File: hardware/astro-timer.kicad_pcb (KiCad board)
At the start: 2 copper layers, 65.8 x 41.4 mm, 29 parts, among them J1 AVR-ISP-6, J2 AudioJack3, Q1 Q_NPN_BEC, Q2 Q_NPN_BEC, SW1 SW_SPST, SW2 SW_Push, SW3 SW_Push, SW4 Rotary_Encoder_Switch, U1 ATmega328P-AU, Y1 Crystal

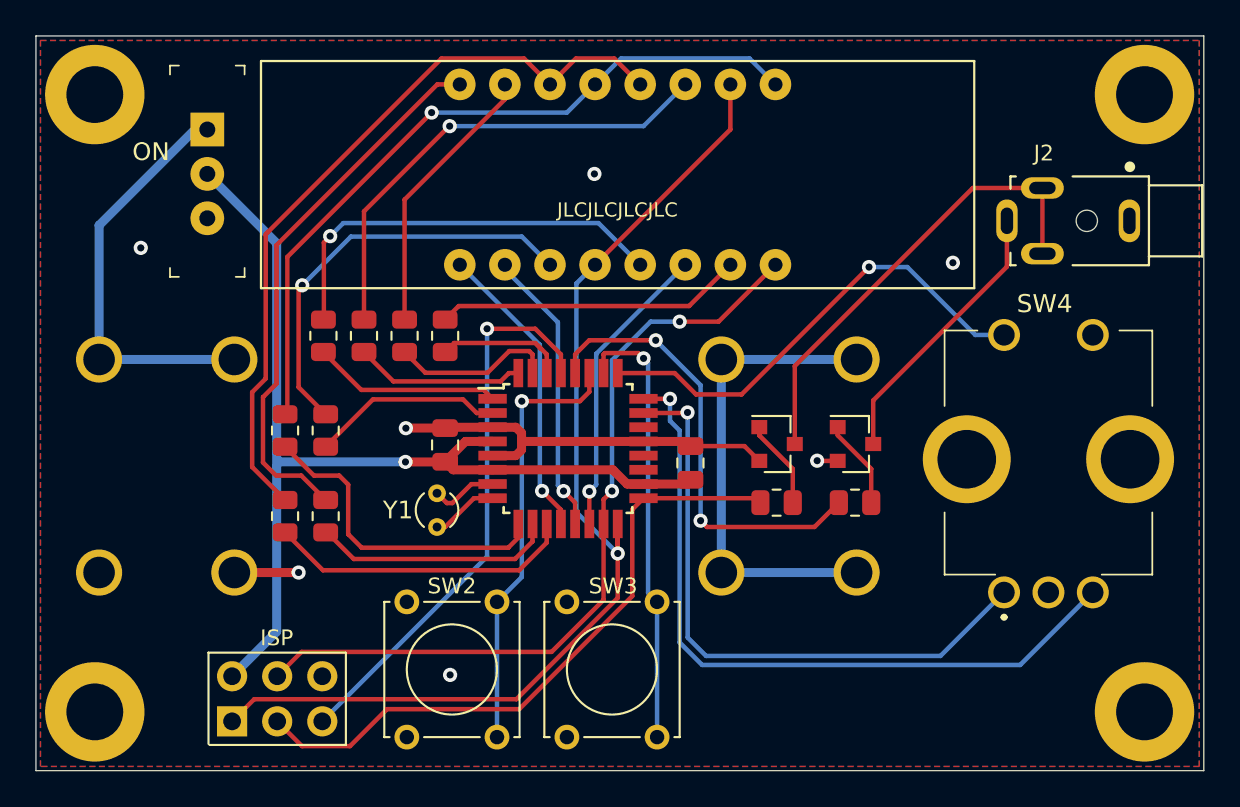
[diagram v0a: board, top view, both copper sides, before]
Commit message: add RC filter circuit for rotary encoder
seems to work pretty well on a breadboard anyway
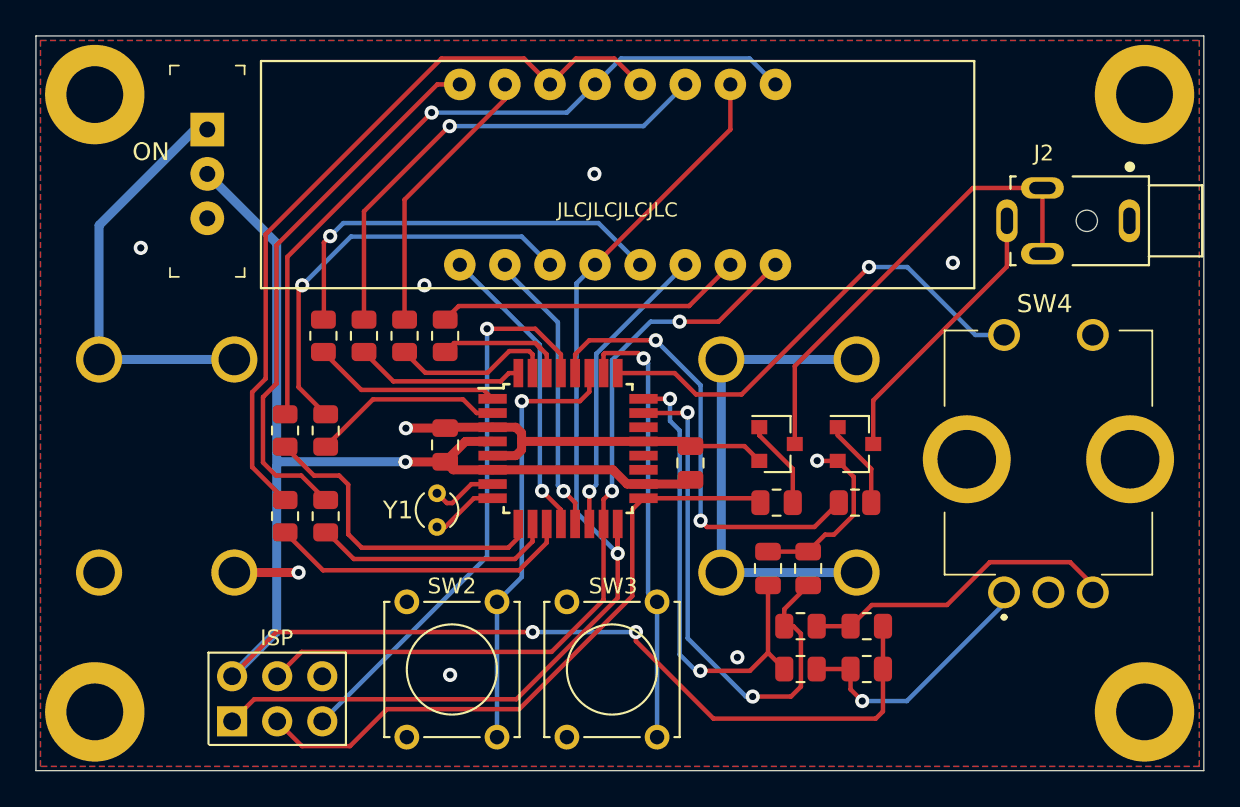
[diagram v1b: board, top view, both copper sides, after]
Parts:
- added C3: 10nF, Capacitor_SMD:C_0805_2012Metric, F.Cu at (123.7, 116.8)
- added C4: 10nF, Capacitor_SMD:C_0805_2012Metric, F.Cu at (125.9, 116.8)
- added R11: 10K, Resistor_SMD:R_0805_2012Metric, F.Cu at (125.5, 120.1)
- added R12: 10K, Resistor_SMD:R_0805_2012Metric, F.Cu at (125.5, 122.5)
- added R13: 10K, Resistor_SMD:R_0805_2012Metric, F.Cu at (129.2, 120.1)
- added R14: 10K, Resistor_SMD:R_0805_2012Metric, F.Cu at (129.2, 122.5)
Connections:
- SW4 pad A: /enc_a -> Net-(R12-Pad1)
- SW4 pad B: /enc_b -> Net-(R11-Pad1)
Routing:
- net VCC: track 58.3 -> 103.2 mm, vias 1 -> 3
- net Net-(R11-Pad1): track 0.00 -> 18.0 mm
- net Net-(R12-Pad1): track 0.00 -> 14.9 mm, vias 0 -> 1
- net /enc_b: track 40.9 -> 27.0 mm, vias 1 -> 2
- net GND: track 28.1 -> 37.2 mm, vias 7 -> 9
- net /enc_a: track 34.9 -> 30.1 mm, vias 1 -> 2

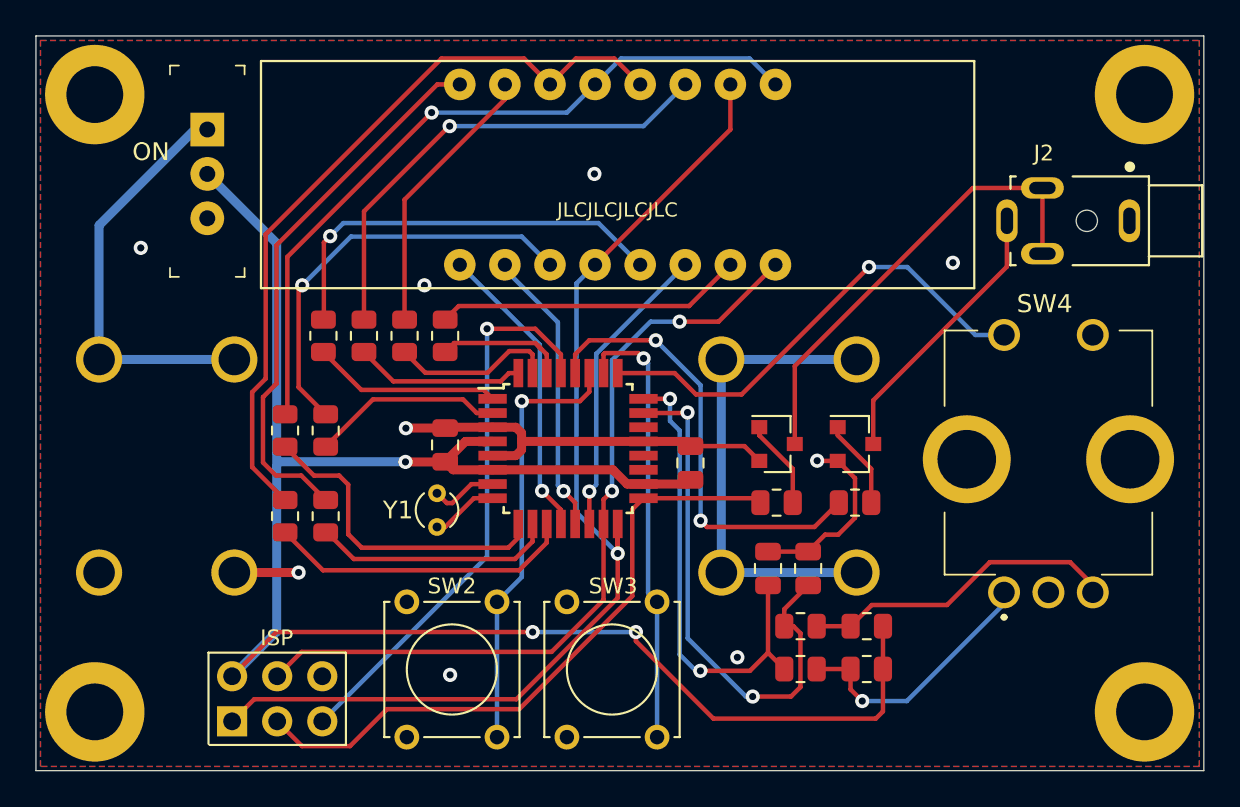
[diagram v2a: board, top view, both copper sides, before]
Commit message: felt a bit uncomfortable routing a trace under an 0805
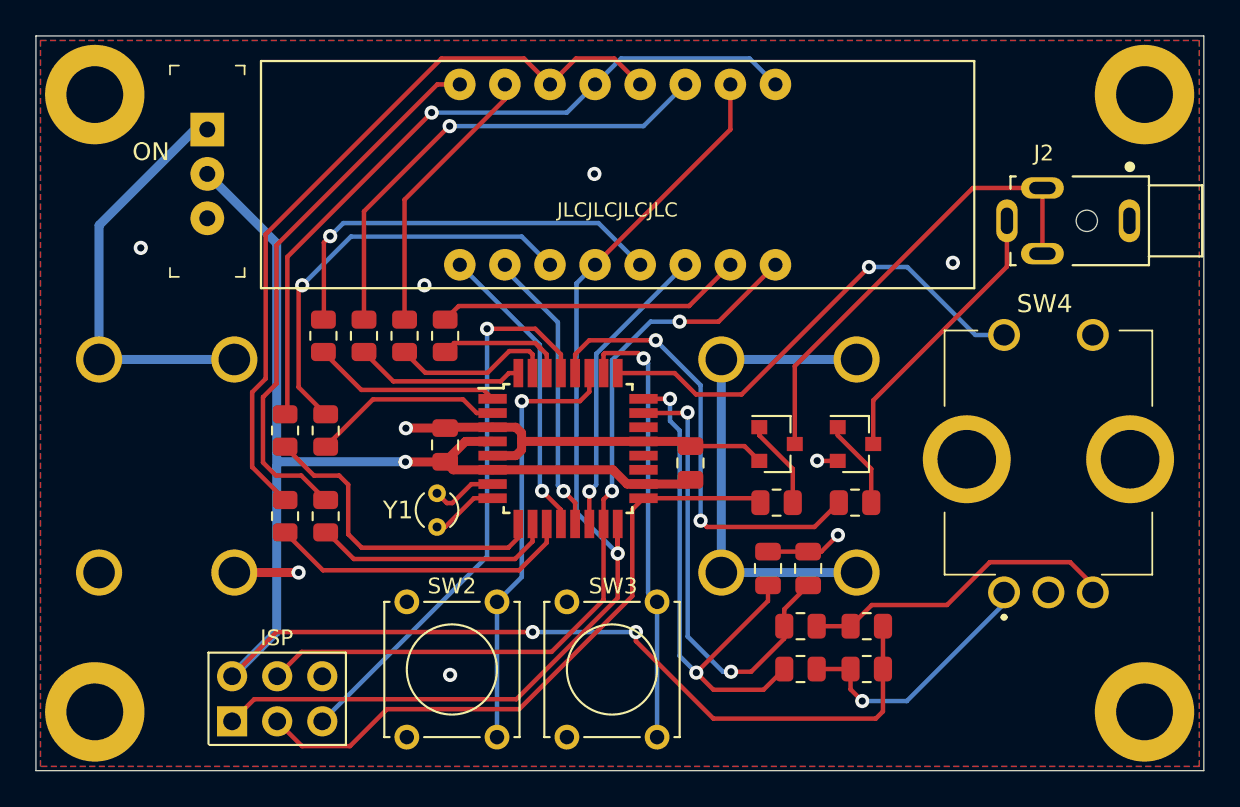
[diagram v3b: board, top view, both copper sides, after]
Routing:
- net GND: track 37.4 -> 32.4 mm
- net /enc_a: track 30.1 -> 25.7 mm
- net /enc_b: track 27.0 -> 30.0 mm

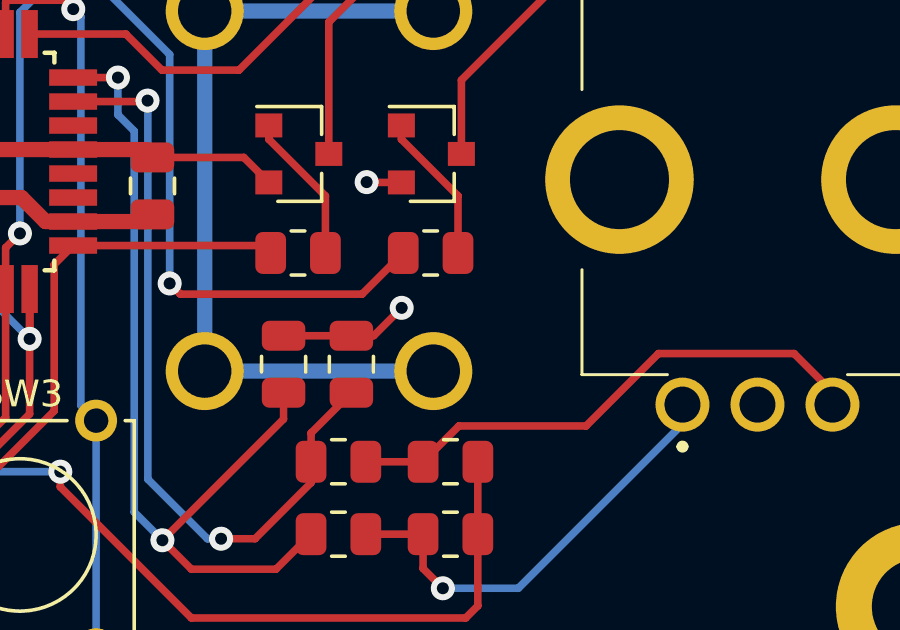
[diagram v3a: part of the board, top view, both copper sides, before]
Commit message: lol whoops that via can't be there
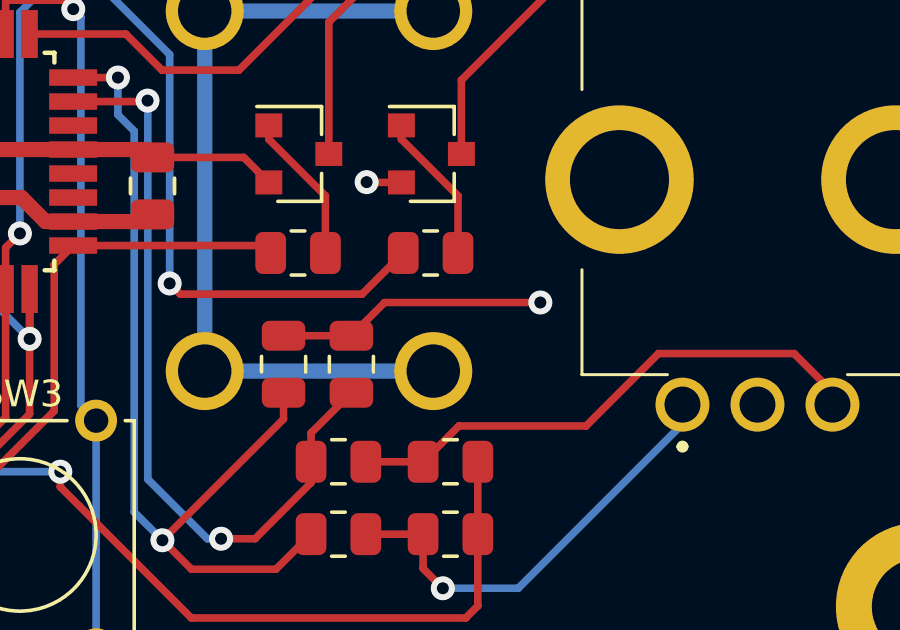
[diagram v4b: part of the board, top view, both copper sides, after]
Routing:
- net GND: track 32.4 -> 37.1 mm

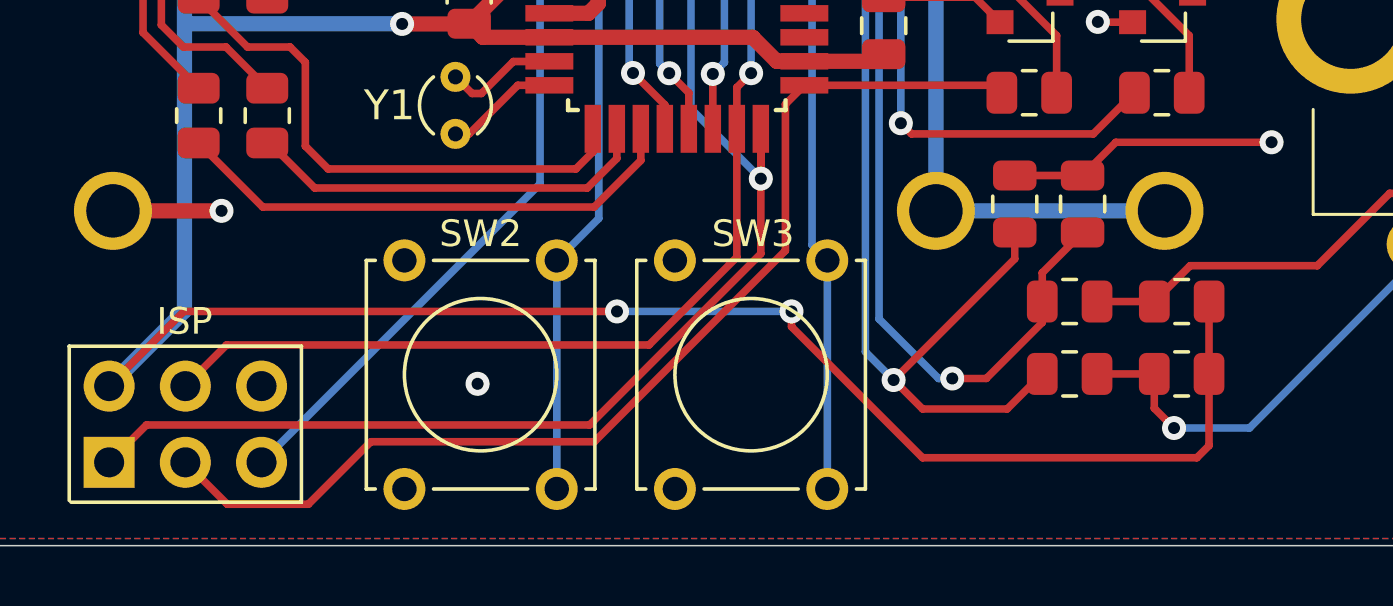
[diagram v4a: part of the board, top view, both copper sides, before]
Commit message: add 10K external pullup on ~RESET
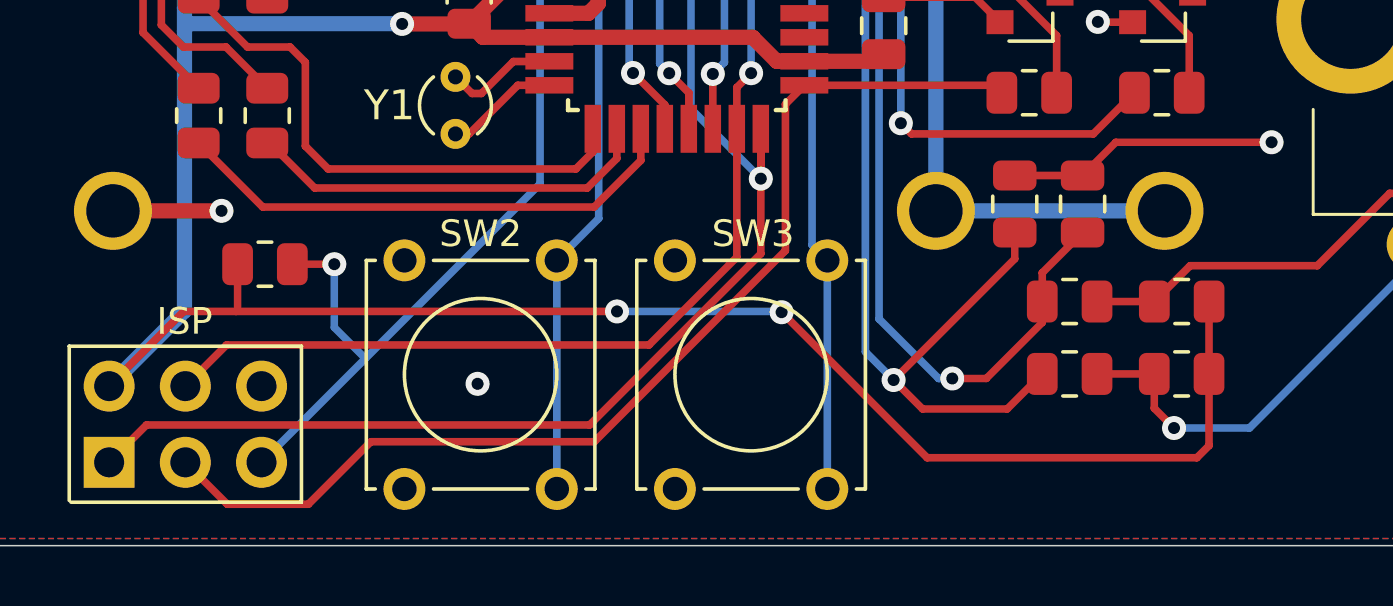
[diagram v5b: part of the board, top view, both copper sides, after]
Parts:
- added R15: 10K, Resistor_SMD:R_0805_2012Metric, F.Cu at (98.7, 118.8)
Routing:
- net /rst: track 31.8 -> 36.7 mm, vias 1 -> 2
- net VCC: track 103.2 -> 104.5 mm

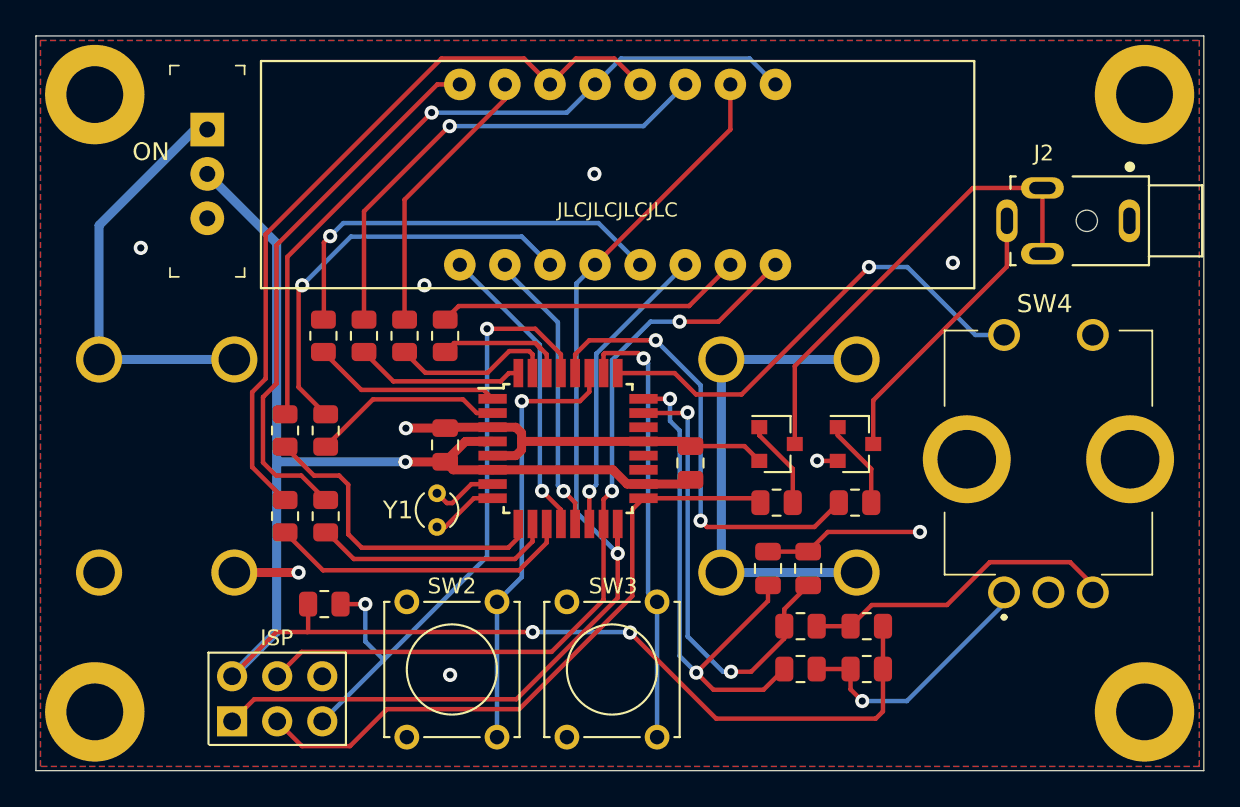
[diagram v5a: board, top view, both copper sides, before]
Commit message: use more common 0603 package for low-current resistors
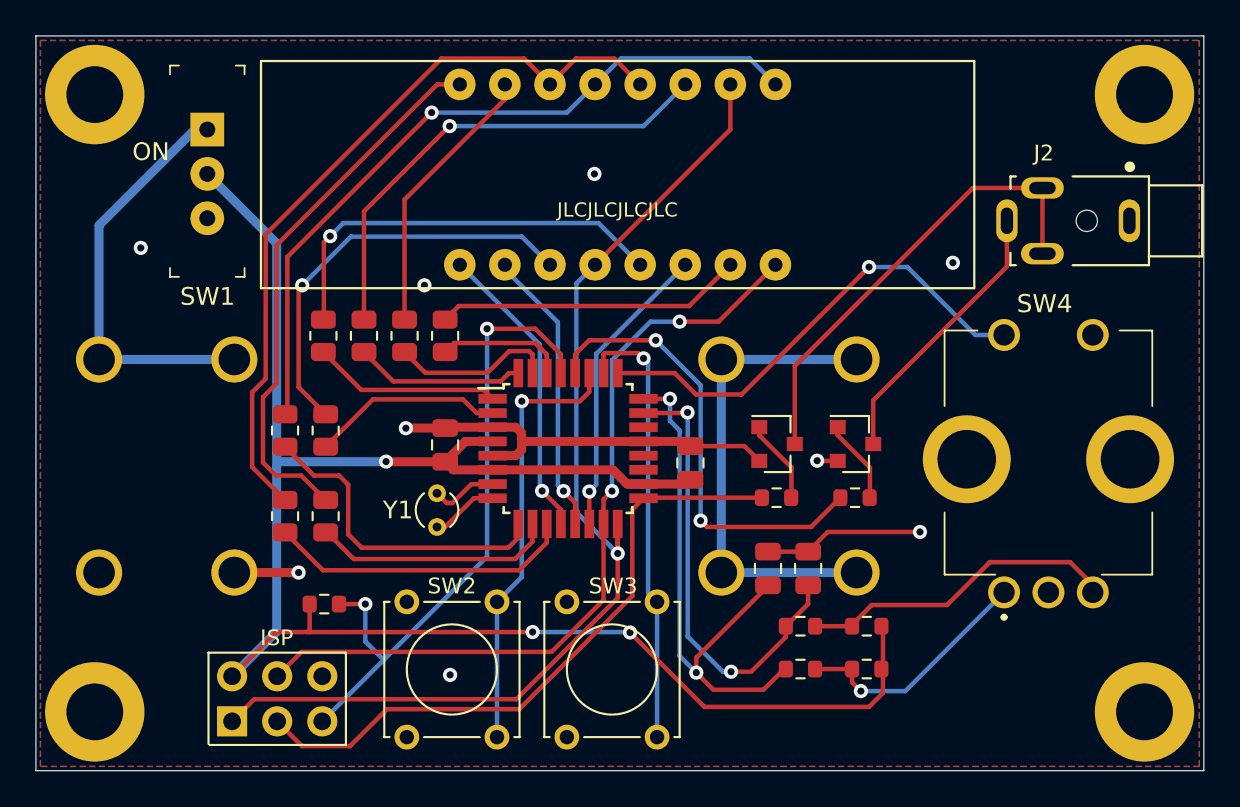
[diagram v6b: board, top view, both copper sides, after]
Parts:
- R10, R11, R12, R13, R14, R15, R9: footprint Resistor_SMD:R_0805_2012Metric -> Resistor_SMD:R_0603_1608Metric
- moved R10 0.28 mm to (128.6, 112.8)
- moved R9 0.28 mm to (124.1, 112.8)
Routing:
- net VCC: track 104.5 -> 103.4 mm
- net Net-(R12-Pad1): track 14.9 -> 13.9 mm
